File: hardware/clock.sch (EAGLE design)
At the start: 9 parts, among them IC2 PCF2123TSSOP14, P1 FSM4JSMA-SMD, P2 FSM4JSMA-SMD, X2 CRYSTALTFORK_SMD

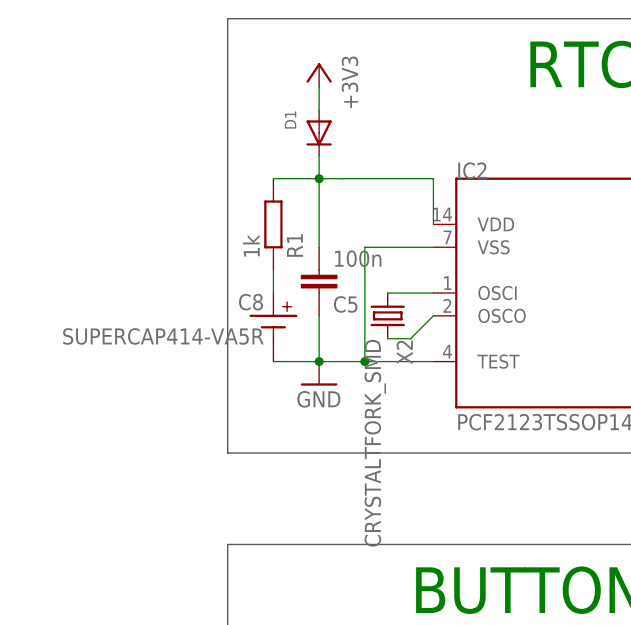
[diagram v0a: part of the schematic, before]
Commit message: changed supercap to a bigger one
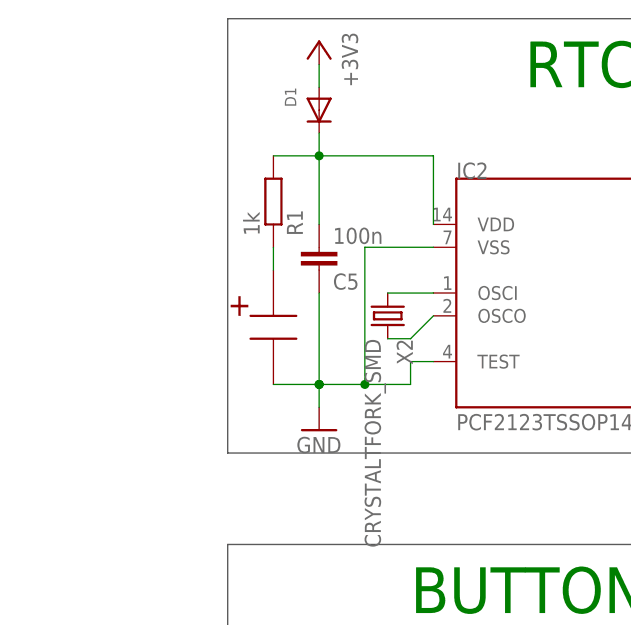
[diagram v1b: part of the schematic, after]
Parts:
- removed C8: SUPERCAP414-VA5R, jocki:SUPERCAP414-VA5R
- added U$1: DCK-3R3E224U-E, jocki:DCK-3R3E224U-E
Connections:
- removed net N$9: C8.PLUS, R1.1
- new net N$1: R1.1, U$1.+
- net GND: now also U$1.-; no longer C8.MINUS
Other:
- moved on the sheet: C5, D1, R1
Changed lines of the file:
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@@
 <part name="X2" library="jocki" deviceset="CRYSTAL" device="TFORK_SMD"/>
 <part name="D1" library="adafruit" deviceset="DIODE" device="SOD-523"/>
-<part name="GND2" library="supply1" deviceset="GND" device=""/>
 <part name="+3V2" library="supply1" deviceset="+3V3" device=""/>
-<part name="C8" library="jocki" deviceset="SUPERCAP" device="414-VA5R"/>
 <part name="R1" library="rcl" deviceset="R-EU_" device="R0603" value="1k"/>
 <part name="C5" library="rcl" deviceset="C-EU" device="C0603K" value="100n"/>
@@
 <part name="GND1" library="supply1" deviceset="GND" device=""/>
 <part name="GND3" library="supply1" deviceset="GND" device=""/>
+<part name="U$1" library="jocki" deviceset="DCK-3R3E224U-E" device=""/>
+<part name="GND2" library="supply1" deviceset="GND" device=""/>
 </parts>
 <sheets>
@@
 <instance part="IC2" gate="G$1" x="134.62" y="114.3"/>
 <instance part="X2" gate="G$1" x="111.76" y="111.76" rot="R270"/>
-<instance part="D1" gate="G$1" x="104.14" y="132.08" rot="MR270"/>
-<instance part="GND2" gate="1" x="104.14" y="104.14"/>
-<instance part="+3V2" gate="G$1" x="104.14" y="139.7" rot="MR0"/>
-<instance part="C8" gate="A" x="99.06" y="111.76" rot="MR0"/>
-<instance part="R1" gate="G$1" x="99.06" y="121.92" rot="MR90"/>
-<instance part="C5" gate="G$1" x="104.14" y="114.3" rot="MR180"/>
+<instance part="D1" gate="G$1" x="104.14" y="134.62" rot="MR270"/>
+<instance part="+3V2" gate="G$1" x="104.14" y="142.24" rot="MR0"/>
+<instance part="R1" gate="G$1" x="99.06" y="124.46" rot="MR90"/>
+<instance part="C5" gate="G$1" x="104.14" y="116.84" rot="MR180"/>
 <instance part="+3V6" gate="G$1" x="157.48" y="127" rot="MR0"/>
 <instance part="P1" gate="G$1" x="127" y="68.58" rot="R270"/>
@@
 <instance part="GND1" gate="1" x="185.42" y="93.98" rot="R180"/>
 <instance part="GND3" gate="1" x="111.76" y="53.34"/>
+<instance part="U$1" gate="G$1" x="99.06" y="109.22"/>
+<instance part="GND2" gate="1" x="104.14" y="99.06"/>
 </instances>
 <busses>
@@
 </net>
 <net name="GND" class="0">
-<segment>
-<pinref part="GND2" gate="1" pin="GND"/>
-<pinref part="C8" gate="A" pin="MINUS"/>
-<wire x1="99.06" y1="106.68" x2="104.14" y2="106.68" width="0.1524" layer="91"/>
-<pinref part="C5" gate="G$1" pin="1"/>
-<wire x1="104.14" y1="106.68" x2="104.14" y2="111.76" width="0.1524" layer="91"/>
-<junction x="104.14" y="106.68"/>
-<wire x1="104.14" y1="106.68" x2="109.22" y2="106.68" width="0.1524" layer="91"/>
-<wire x1="109.22" y1="106.68" x2="109.22" y2="119.38" width="0.1524" layer="91"/>
-<pinref part="IC2" gate="G$1" pin="VSS"/>
-<wire x1="109.22" y1="119.38" x2="116.84" y2="119.38" width="0.1524" layer="91"/>
-<pinref part="IC2" gate="G$1" pin="TEST"/>
-<wire x1="109.22" y1="106.68" x2="116.84" y2="106.68" width="0.1524" layer="91"/>
-<junction x="109.22" y="106.68"/>
-</segment>
 <segment>
 <pinref part="P1" gate="G$1" pin="P"/>
@@
 <wire x1="185.42" y1="88.9" x2="195.58" y2="88.9" width="0.1524" layer="91"/>
 </segment>
+<segment>
+<pinref part="U$1" gate="G$1" pin="-"/>
+<pinref part="GND2" gate="1" pin="GND"/>
+<wire x1="99.06" y1="104.14" x2="104.14" y2="104.14" width="0.1524" layer="91"/>
+<wire x1="104.14" y1="104.14" x2="104.14" y2="101.6" width="0.1524" layer="91"/>
+<pinref part="C5" gate="G$1" pin="1"/>
+<wire x1="104.14" y1="104.14" x2="104.14" y2="114.3" width="0.1524" layer="91"/>
+<wire x1="104.14" y1="104.14" x2="109.22" y2="104.14" width="0.1524" layer="91"/>
+<wire x1="109.22" y1="104.14" x2="109.22" y2="119.38" width="0.1524" layer="91"/>
+<pinref part="IC2" gate="G$1" pin="VSS"/>
+<wire x1="109.22" y1="119.38" x2="116.84" y2="119.38" width="0.1524" layer="91"/>
+<junction x="104.14" y="104.14"/>
+<junction x="104.14" y="104.14"/>
+<pinref part="IC2" gate="G$1" pin="TEST"/>
+<wire x1="116.84" y1="106.68" x2="114.3" y2="106.68" width="0.1524" layer="91"/>
+<wire x1="114.3" y1="106.68" x2="114.3" y2="104.14" width="0.1524" layer="91"/>
+<wire x1="114.3" y1="104.14" x2="109.22" y2="104.14" width="0.1524" layer="91"/>
+<junction x="109.22" y="104.14"/>
+</segment>
 </net>
 <net name="+3V3" class="0">
@@
 <pinref part="D1" gate="G$1" pin="A"/>
 <pinref part="+3V2" gate="G$1" pin="+3V3"/>
-<wire x1="104.14" y1="134.62" x2="104.14" y2="137.16" width="0.1524" layer="91"/>
+<wire x1="104.14" y1="137.16" x2="104.14" y2="139.7" width="0.1524" layer="91"/>
 </segment>
 <segment>
@@
 <segment>
 <pinref part="C5" gate="G$1" pin="2"/>
-<wire x1="104.14" y1="127" x2="104.14" y2="119.38" width="0.1524" layer="91"/>
+<wire x1="104.14" y1="129.54" x2="104.14" y2="121.92" width="0.1524" layer="91"/>
 <pinref part="D1" gate="G$1" pin="C"/>
-<wire x1="104.14" y1="127" x2="104.14" y2="129.54" width="0.1524" layer="91"/>
+<wire x1="104.14" y1="129.54" x2="104.14" y2="132.08" width="0.1524" layer="91"/>
 <pinref part="R1" gate="G$1" pin="2"/>
-<wire x1="104.14" y1="127" x2="99.06" y2="127" width="0.1524" layer="91"/>
-<wire x1="104.14" y1="127" x2="106.68" y2="127" width="0.1524" layer="91"/>
-<junction x="104.14" y="127"/>
+<wire x1="104.14" y1="129.54" x2="99.06" y2="129.54" width="0.1524" layer="91"/>
+<junction x="104.14" y="129.54"/>
 <pinref part="IC2" gate="G$1" pin="VDD"/>
-<wire x1="106.68" y1="127" x2="116.84" y2="127" width="0.1524" layer="91"/>
-<wire x1="116.84" y1="127" x2="116.84" y2="121.92" width="0.1524" layer="91"/>
-</segment>
-</net>
-<net name="N$9" class="0">
-<segment>
-<pinref part="R1" gate="G$1" pin="1"/>
-<pinref part="C8" gate="A" pin="PLUS"/>
-<wire x1="99.06" y1="116.84" x2="99.06" y2="114.3" width="0.1524" layer="91"/>
+<wire x1="104.14" y1="129.54" x2="116.84" y2="129.54" width="0.1524" layer="91"/>
+<wire x1="116.84" y1="129.54" x2="116.84" y2="121.92" width="0.1524" layer="91"/>
 </segment>
 </net>
@@
 </segment>
 </net>
+<net name="N$1" class="0">
+<segment>
+<pinref part="R1" gate="G$1" pin="1"/>
+<pinref part="U$1" gate="G$1" pin="+"/>
+<wire x1="99.06" y1="119.38" x2="99.06" y2="116.84" width="0.1524" layer="91"/>
+</segment>
+</net>
